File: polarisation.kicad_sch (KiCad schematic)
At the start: 31 parts, among them J1 HV_BIAS_IN, Q6 BSS127I, Q7 BSS127I, U10 ISO7710, U11 AMC0311R, U21 MCP6001

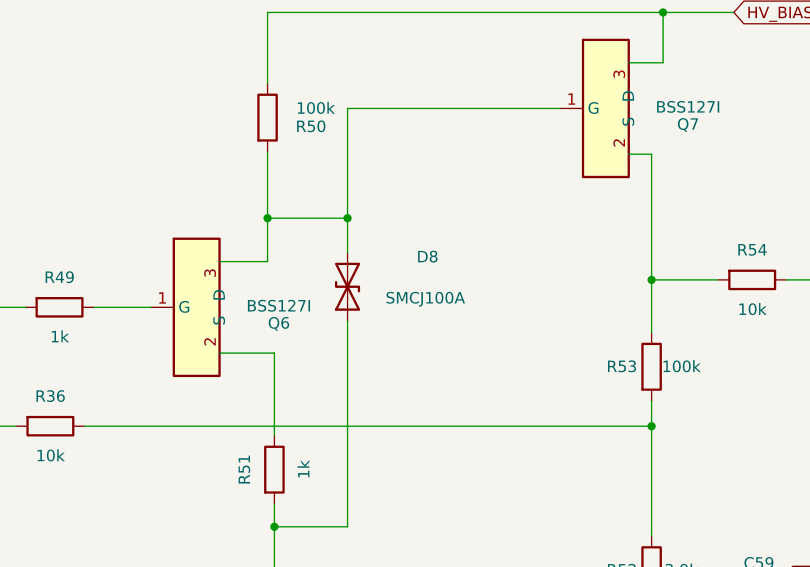
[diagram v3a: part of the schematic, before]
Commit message: Dissipation Reg1/Reg2, vias Q1 ajustes, retouches TVS
- Reg1 (LM317M) et Reg2 (MCP1703-3302) : connexion solide (zone_connect
  solid) sur les pastilles sortie/masse ; petite surface de dissipation
  RAIL_3V3_PRI sur B.Cu sous Reg2.
- Q1 : 18->12 vias thermiques, 6 retirees car elles barraient le passage
  de la zone RAIL_8V25 sur In2.Cu. Impact thermique verifie negligeable
  a la dissipation reelle de Q1 (~0,7W, simulation), encore confortable
  au cas pessimiste 2,1W/50degC (toutes pertes dans Q1, Rth(j-c) Infineon
  IPD050N10N5 = 1K/W max, Tj max 175degC).
- Via VOUT_N repositionne (143.87/87.61) pour stitcher F.Cu<->In1.Cu sans
  chevaucher la pastille du condensateur voisin ni les zones GND(B.Cu)/
  RAIL_3V3_PRI(In2.Cu).
- D3/D5/D8 (TVS) : SMCJ*->SMBJ* (boitier D_SMC->D_SMB).

DRC : 0 erreur (3 avertissements lib_footprint_mismatch bénins connus).

Co-Authored-By: Claude Sonnet 5 <noreply@anthropic.com>
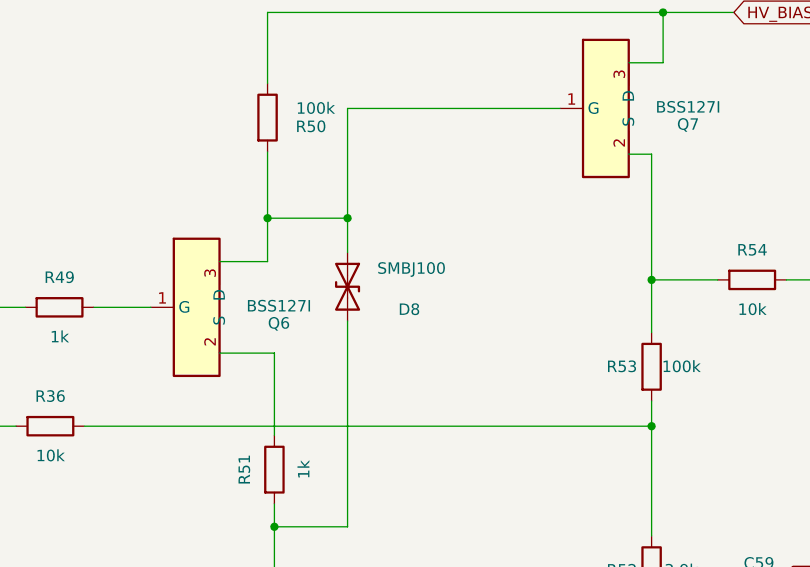
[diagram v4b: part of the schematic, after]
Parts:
- D8: value SMCJ100A -> SMBJ100; footprint Diode_SMD:D_SMC -> Diode_SMD:D_SMB
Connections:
- net GND: now also D8.2 (A2); no longer D8.1 (A1)
- net at Q6.3 (D), Q7.1 (G), R50.2: now also D8.1 (A1); no longer D8.2 (A2)
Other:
- moved on the sheet: D8
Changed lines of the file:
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@@
 	(symbol
 		(lib_id "Device:D_TVS")
-		(at 156.718 132.842 90)
+		(at 156.718 132.842 270)
 		(unit 1)
 		(body_style 1)
@@
 		(dnp no)
 		(property "Reference" "D8"
-			(at 165.608 129.54 270)
+			(at 163.576 135.382 270)
 			(show_name no)
 			(do_not_autoplace no)
@@
 			)
 		)
-		(property "Value" "SMCJ100A"
-			(at 165.354 134.112 270)
+		(property "Value" "SMBJ100"
+			(at 163.83 130.81 270)
 			(show_name no)
 			(do_not_autoplace no)
@@
 			)
 		)
-		(property "Footprint" "Diode_SMD:D_SMC"
+		(property "Footprint" "Diode_SMD:D_SMB"
 			(at 156.718 132.842 0)
 			(hide yes)
